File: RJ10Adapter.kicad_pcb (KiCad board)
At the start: 2 copper layers, 73.1 x 18.3 mm, 16 parts, among them J1 RJ10, J2 Conn_01x06_Male, J3 USB_B_Micro, SW1 SW_Push, U1 AMS1117-3.3, U2 ESP-12F

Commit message: Changed RX and TX
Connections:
- J1 pad 2: /RX -> /TX
- J1 pad 3: /TX -> /RX
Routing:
- net /TX: track 37.5 -> 32.1 mm
- net /RX: track 32.4 -> 29.5 mm
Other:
- board text added: "v1.3"
- board text removed: "v1.2"
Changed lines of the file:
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@@
     (thickness 1.6)
     (drawings 30)
-    (tracks 125)
+    (tracks 118)
     (zones 0)
     (modules 16)
@@
   (title_block
     (title "RJ FTDI Adapter")
-    (date 2019-10-24)
-    (rev 1.2)
+    (date 2020-08-09)
+    (rev 1.3)
     (company haus-automatisierung.com)
     (comment 1 "Matthias Kleine")
@@
       (net 2 /Vin))
     (pad 2 thru_hole circle (at 6.565 0.6517) (size 1.524 1.524) (drill 0.9) (layers *.Cu *.Mask)
-      (net 27 /RX))
-    (pad 3 thru_hole circle (at 9.105 -0.6183) (size 1.524 1.524) (drill 0.9) (layers *.Cu *.Mask)
       (net 28 /TX))
+    (pad 3 thru_hole circle (at 9.105 -0.6183) (size 1.524 1.524) (drill 0.9) (layers *.Cu *.Mask)
+      (net 27 /RX))
     (pad 4 thru_hole rect (at 6.565 -1.8883) (size 1.524 1.524) (drill 0.9) (layers *.Cu *.Mask)
       (net 1 GND))
@@
     (arrow2b (pts (xy 142.125519 83.312492) (xy 143.254081 82.730041)))
   )
-  (gr_text v1.2 (at 184.531 91.948 90) (layer B.SilkS)
+  (gr_text v1.3 (at 184.531 91.948 90) (layer B.SilkS)
     (effects (font (size 1 1) (thickness 0.2)) (justify right mirror))
   )
@@
     (effects (font (size 0.8 0.8) (thickness 0.15)) (justify right))
   )
-  (gr_text v1.2 (at 140.6017 88.646) (layer F.SilkS)
+  (gr_text v1.3 (at 140.6017 88.646) (layer F.SilkS)
     (effects (font (size 1 1) (thickness 0.2)) (justify right))
   )
@@
   (segment (start 143.6203 98.4417) (end 144.272 97.79) (width 0.25) (layer F.Cu) (net 2))
   (segment (start 139.153 98.4417) (end 143.6203 98.4417) (width 0.25) (layer F.Cu) (net 2))
-  (segment (start 145.121999 96.940001) (end 144.272 97.79) (width 0.25) (layer F.Cu) (net 2))
-  (segment (start 145.447001 92.361997) (end 145.447001 96.614999) (width 0.25) (layer F.Cu) (net 2))
-  (segment (start 145.447001 96.614999) (end 145.121999 96.940001) (width 0.25) (layer F.Cu) (net 2))
-  (segment (start 148.888998 88.92) (end 145.447001 92.361997) (width 0.25) (layer F.Cu) (net 2))
-  (segment (start 149.774 88.92) (end 148.888998 88.92) (width 0.25) (layer F.Cu) (net 2))
   (segment (start 177.7275 98.434) (end 177.7275 98.298) (width 0.25) (layer F.Cu) (net 2))
   (segment (start 184.379 91.059) (end 178.079 91.059) (width 0.25) (layer F.Cu) (net 2))
@@
   (via (at 162.56 99.06) (size 0.8) (drill 0.4) (layers F.Cu B.Cu) (net 2))
   (segment (start 160.02 96.52) (end 162.56 99.06) (width 0.25) (layer B.Cu) (net 2))
+  (segment (start 144.272 97.79) (end 146.6 95.462) (width 0.25) (layer F.Cu) (net 2))
+  (segment (start 146.6 95.462) (end 146.6 90.4) (width 0.25) (layer F.Cu) (net 2))
+  (segment (start 148.08 88.92) (end 149.774 88.92) (width 0.25) (layer F.Cu) (net 2))
+  (segment (start 146.6 90.4) (end 148.08 88.92) (width 0.25) (layer F.Cu) (net 2))
   (segment (start 181.3985 101.0585) (end 182.2455 101.0585) (width 0.25) (layer F.Cu) (net 5))
   (segment (start 179.832 102.625) (end 181.3985 101.0585) (width 0.25) (layer F.Cu) (net 5))
@@
   (segment (start 155.774 103.37) (end 155.774 104.12) (width 0.25) (layer F.Cu) (net 26))
   (segment (start 174.5869 100.42) (end 158.724 100.42) (width 0.25) (layer F.Cu) (net 26))
-  (via (at 159.9565 101.9175) (size 0.8) (drill 0.4) (layers F.Cu B.Cu) (net 27))
-  (segment (start 161.774 103.37) (end 160.3215 101.9175) (width 0.25) (layer F.Cu) (net 27))
-  (segment (start 160.3215 101.9175) (end 159.9565 101.9175) (width 0.25) (layer F.Cu) (net 27))
+  (segment (start 141.0803 95.9017) (end 144.272 92.71) (width 0.25) (layer F.Cu) (net 27))
+  (segment (start 139.153 95.9017) (end 141.0803 95.9017) (width 0.25) (layer F.Cu) (net 27))
+  (via (at 160.2 101.2) (size 0.8) (drill 0.4) (layers F.Cu B.Cu) (net 27))
+  (segment (start 160.2 101.796) (end 160.2 101.2) (width 0.25) (layer F.Cu) (net 27))
+  (segment (start 161.774 103.37) (end 160.2 101.796) (width 0.25) (layer F.Cu) (net 27))
   (segment (start 161.774 104.12) (end 161.774 103.37) (width 0.25) (layer F.Cu) (net 27))
-  (segment (start 150.749 92.71) (end 144.272 92.71) (width 0.25) (layer B.Cu) (net 27))
-  (segment (start 159.9565 101.9175) (end 150.749 92.71) (width 0.25) (layer B.Cu) (net 27))
-  (segment (start 143.069919 92.71) (end 144.272 92.71) (width 0.25) (layer F.Cu) (net 27))
-  (segment (start 137.374999 96.070939) (end 140.735938 92.71) (width 0.25) (layer F.Cu) (net 27))
-  (segment (start 140.735938 92.71) (end 143.069919 92.71) (width 0.25) (layer F.Cu) (net 27))
-  (segment (start 137.374999 96.409701) (end 137.374999 96.070939) (width 0.25) (layer F.Cu) (net 27))
-  (segment (start 136.613 97.1717) (end 137.374999 96.409701) (width 0.25) (layer F.Cu) (net 27))
-  (segment (start 143.6203 95.9017) (end 144.272 95.25) (width 0.25) (layer F.Cu) (net 28))
-  (segment (start 139.153 95.9017) (end 143.6203 95.9017) (width 0.25) (layer F.Cu) (net 28))
-  (segment (start 162.3215 101.9175) (end 161.906502 101.9175) (width 0.25) (layer F.Cu) (net 28))
-  (via (at 161.4805 101.9175) (size 0.8) (drill 0.4) (layers F.Cu B.Cu) (net 28))
-  (segment (start 161.906502 101.9175) (end 161.4805 101.9175) (width 0.25) (layer F.Cu) (net 28))
-  (segment (start 163.774 103.37) (end 162.3215 101.9175) (width 0.25) (layer F.Cu) (net 28))
-  (segment (start 139.914999 95.139701) (end 139.153 95.9017) (width 0.25) (layer B.Cu) (net 28))
-  (segment (start 143.519701 91.534999) (end 139.914999 95.139701) (width 0.25) (layer B.Cu) (net 28))
-  (segment (start 151.097999 91.534999) (end 143.519701 91.534999) (width 0.25) (layer B.Cu) (net 28))
-  (segment (start 161.4805 101.9175) (end 151.097999 91.534999) (width 0.25) (layer B.Cu) (net 28))
+  (segment (start 152.762 101.2) (end 144.272 92.71) (width 0.25) (layer B.Cu) (net 27))
+  (segment (start 160.2 101.2) (end 152.762 101.2) (width 0.25) (layer B.Cu) (net 27))
+  (segment (start 142.3503 97.1717) (end 144.272 95.25) (width 0.25) (layer F.Cu) (net 28))
+  (segment (start 136.613 97.1717) (end 142.3503 97.1717) (width 0.25) (layer F.Cu) (net 28))
+  (segment (start 162.404 102) (end 162.2 102) (width 0.25) (layer F.Cu) (net 28))
+  (segment (start 163.774 103.37) (end 162.404 102) (width 0.25) (layer F.Cu) (net 28))
+  (via (at 162.2 102) (size 0.8) (drill 0.4) (layers F.Cu B.Cu) (net 28))
   (segment (start 163.774 104.12) (end 163.774 103.37) (width 0.25) (layer F.Cu) (net 28))
+  (segment (start 151.022 102) (end 144.272 95.25) (width 0.25) (layer B.Cu) (net 28))
+  (segment (start 162.2 102) (end 151.022 102) (width 0.25) (layer B.Cu) (net 28))
   (segment (start 153.774 103.37) (end 153.774 104.12) (width 0.25) (layer F.Cu) (net 29))
   (segment (start 173.6 89.635) (end 172.976628 90.258372) (width 0.25) (layer F.Cu) (net 29))

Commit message: Updated to KiCad 6
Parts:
- J1: footprint halibs:MEBP_44S -> haus-automatisierung:MEBP_44S
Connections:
- J2 pad 2: Net-(J2-Pad2) -> unconnected-(J2-Pad2)
- J2 pad 6: Net-(J2-Pad6) -> unconnected-(J2-Pad6)
- J3 pad 2: Net-(J3-Pad2) -> unconnected-(J3-Pad2)
- J3 pad 3: Net-(J3-Pad3) -> unconnected-(J3-Pad3)
- J3 pad 4: Net-(J3-Pad4) -> unconnected-(J3-Pad4)
- J3 pad 6: Net-(J3-Pad6) -> unconnected-(J3-Pad6)
- U2 pad 1: Net-(U2-Pad1) -> unconnected-(U2-Pad1)
- U2 pad 10: Net-(U2-Pad10) -> unconnected-(U2-Pad10)
- U2 pad 11: Net-(U2-Pad11) -> unconnected-(U2-Pad11)
- U2 pad 12: Net-(U2-Pad12) -> unconnected-(U2-Pad12)
- U2 pad 13: Net-(U2-Pad13) -> unconnected-(U2-Pad13)
- U2 pad 14: Net-(U2-Pad14) -> unconnected-(U2-Pad14)
- U2 pad 19: Net-(U2-Pad19) -> unconnected-(U2-Pad19)
- U2 pad 2: Net-(U2-Pad2) -> unconnected-(U2-Pad2)
- U2 pad 20: Net-(U2-Pad20) -> unconnected-(U2-Pad20)
- U2 pad 4: Net-(U2-Pad4) -> unconnected-(U2-Pad4)
- U2 pad 5: Net-(U2-Pad5) -> unconnected-(U2-Pad5)
- U2 pad 6: Net-(U2-Pad6) -> unconnected-(U2-Pad6)
- U2 pad 7: Net-(U2-Pad7) -> unconnected-(U2-Pad7)
- U2 pad 9: Net-(U2-Pad9) -> unconnected-(U2-Pad9)
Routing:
- net unconnected-(J3-Pad6): track 0.00 -> 10.8 mm
- net Net-(J3-Pad6): track 10.8 -> 0.00 mm
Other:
- net class Default removed
- board text added: "v1.4"

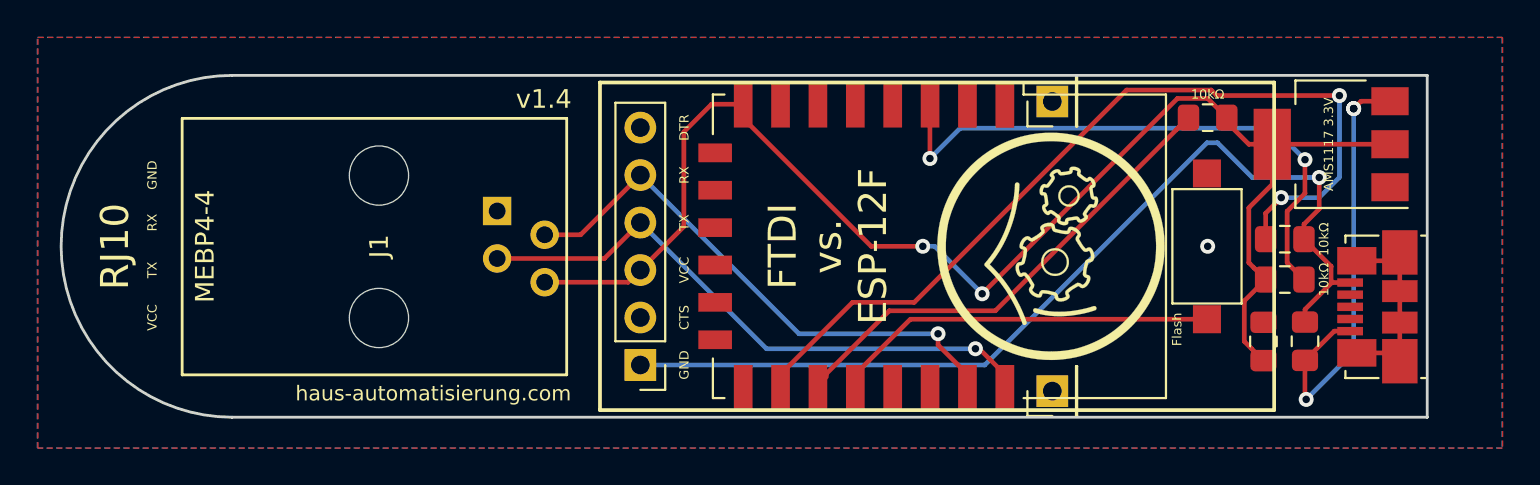
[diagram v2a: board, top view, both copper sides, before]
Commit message: Deleted unconnected tracks
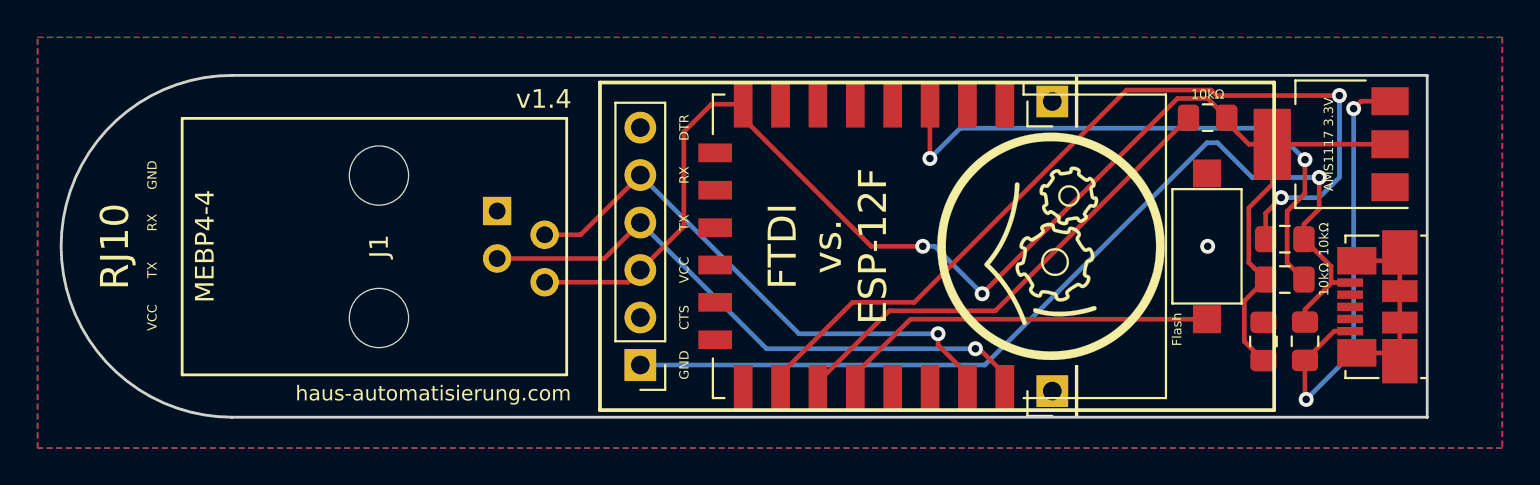
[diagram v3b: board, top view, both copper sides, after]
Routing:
- net Net-(R3-Pad2): track 26.9 -> 25.1 mm
- net +5V: vias 3 -> 2
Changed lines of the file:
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@@
   (segment (start 184.379 91.059) (end 178.079 91.059) (width 0.25) (layer "F.Cu") (net 2))
   (segment (start 149.774 89.67) (end 156.624 96.52) (width 0.25) (layer "F.Cu") (net 2))
-  (segment (start 177.7275 98.434) (end 177.7275 98.298) (width 0.25) (layer "F.Cu") (net 2))
   (segment (start 174.62499 88.60999) (end 173.01001 88.60999) (width 0.25) (layer "F.Cu") (net 2))
   (segment (start 175.65 89.88) (end 175.65 89.635) (width 0.25) (layer "F.Cu") (net 2))
@@
   (segment (start 181.3985 101.0585) (end 182.2455 101.0585) (width 0.25) (layer "F.Cu") (net 5))
   (via (at 179.8955 104.7115) (size 0.8) (drill 0.4) (layers "F.Cu" "B.Cu") (net 5))
-  (via (at 182.4355 89.154) (size 0.8) (drill 0.4) (layers "F.Cu" "B.Cu") (net 5))
   (via (at 182.4355 89.154) (size 0.8) (drill 0.4) (layers "F.Cu" "B.Cu") (net 5))
   (segment (start 182.4355 102.1715) (end 182.4355 89.154) (width 0.25) (layer "B.Cu") (net 5))
@@
   (segment (start 157.589008 99.96999) (end 154.22401 103.334988) (width 0.25) (layer "F.Cu") (net 29))
   (segment (start 173.6 89.635) (end 163.26501 99.96999) (width 0.25) (layer "F.Cu") (net 29))
-  (segment (start 154.22401 103.334988) (end 154.22401 103.516986) (width 0.25) (layer "F.Cu") (net 29))
-  (segment (start 153.774 103.37) (end 153.774 104.12) (width 0.25) (layer "F.Cu") (net 29))
-  (segment (start 173.6 89.635) (end 172.976628 90.258372) (width 0.25) (layer "F.Cu") (net 29))
   (segment (start 163.26501 99.96999) (end 157.589008 99.96999) (width 0.25) (layer "F.Cu") (net 29))
   (zone (net 1) (net_name "GND") (layer "F.Cu") (hatch edge 0.508)

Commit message: v1.4
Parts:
- C1, C2: footprint Capacitor_SMD:C_0805_2012Metric_Pad1.15x1.40mm_HandSolder -> Capacitor_SMD:C_0805_2012Metric_Pad1.18x1.45mm_HandSolder
- R1, R2, R3: footprint Resistor_SMD:R_0805_2012Metric_Pad1.15x1.40mm_HandSolder -> Resistor_SMD:R_0805_2012Metric_Pad1.20x1.40mm_HandSolder
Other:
- board text removed: "v1.3"
